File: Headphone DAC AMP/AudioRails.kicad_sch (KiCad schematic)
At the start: 19 parts, among them U12 TPS74501PDRVR, U14 ADP7185ACPZN-R7

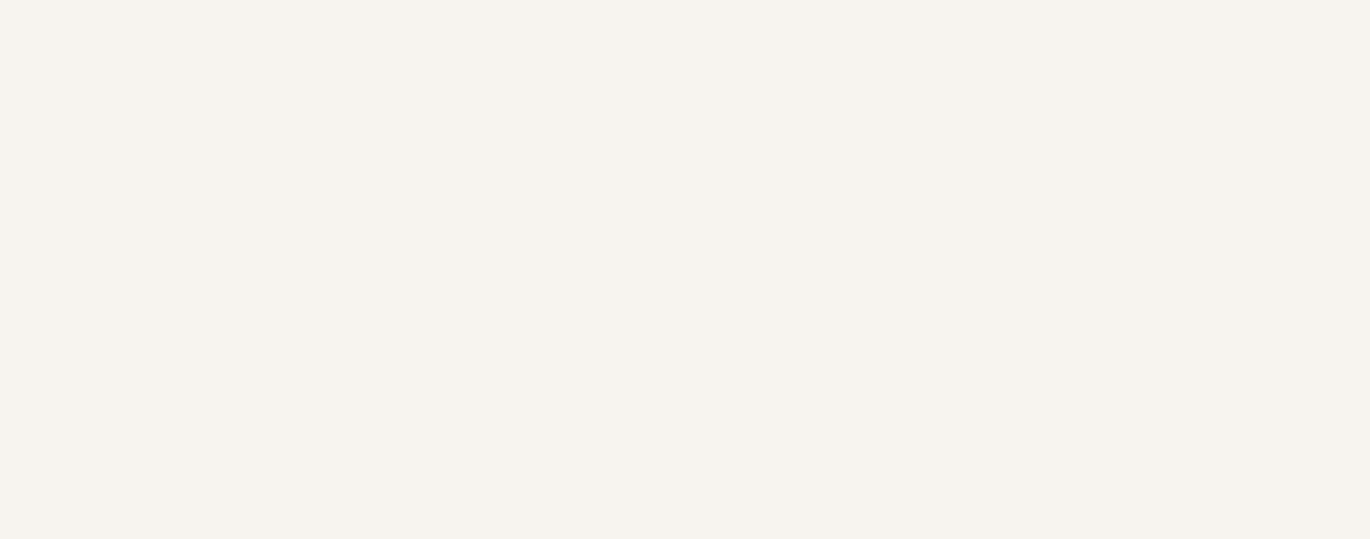
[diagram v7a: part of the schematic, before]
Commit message: Add TPS7A39 regulator and update power rail wiring
Added the TPS7A39 dual LDO voltage regulator symbol to AudioRails.kicad_sch and updated schematic wiring and junctions to integrate the new power supply. Adjusted connections and added new wires and junctions to support the updated power distribution.
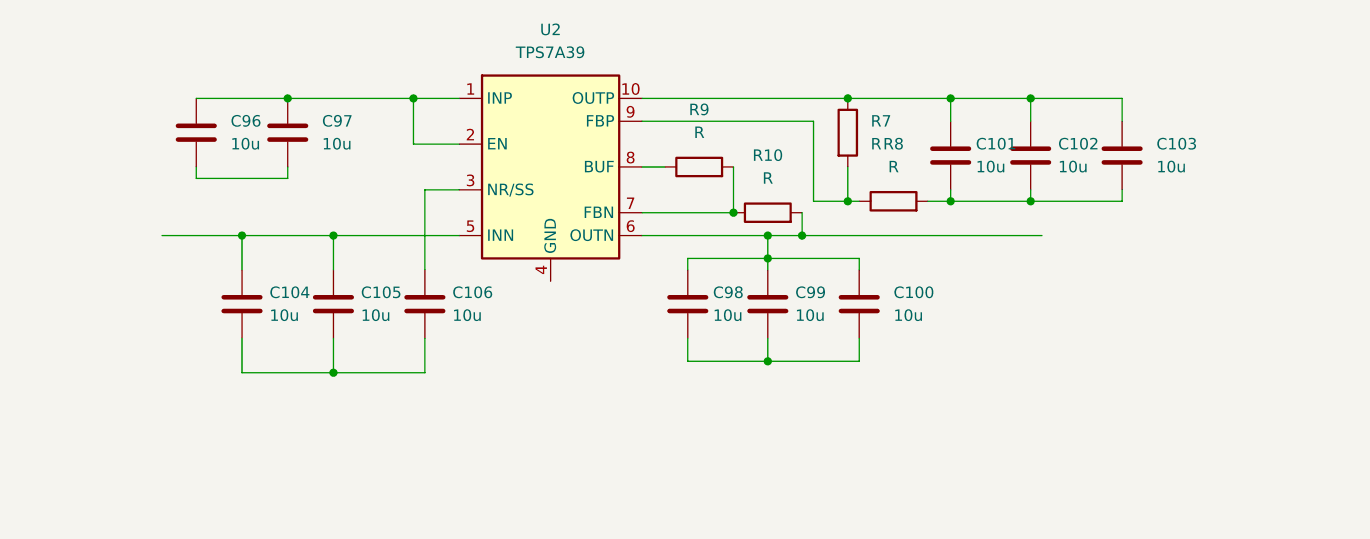
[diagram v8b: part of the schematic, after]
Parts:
- added C100, C101, C102, C103, C104, C105, C106, C96, C97, C98, C99: 10u, Capacitor_SMD:C_0603_1608Metric_Pad1.08x0.95mm_HandSolder, symbol Device:C
- added R10, R7, R8, R9: R, symbol Device:R
- added U2: TPS7A39, Package_SON:Texas_S-PVSON-N10_ThermalVias, symbol Regulator_Linear:TPS7A39
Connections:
- new net: C101.1, C102.1, C103.1, R7.1, U2.10 (OUTP)
- new net: C101.2, C102.2, C103.2, R8.2
- new net: C100.1, C98.1, C99.1, R10.2, U2.6 (OUTN)
- new net: C100.2, C98.2, C99.2
- new net: C96.1, C97.1, U2.1 (INP), U2.2 (EN)
- new net: C96.2, C97.2
- new net: R9.1, U2.8 (BUF)
- new net: R10.1, R9.2, U2.7 (FBN)
- new net: C104.1, C105.1, U2.5 (INN)
- new net: C104.2, C105.2, C106.2
- new net: R7.2, R8.1, U2.9 (FBP)
- new net: C106.1, U2.3 (NR/SS)
- new net: U2.11 (GND), U2.4 (GND)
